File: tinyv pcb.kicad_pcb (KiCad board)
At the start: 2 copper layers, 208.8 x 80.2 mm, 102 parts, among them J1 JST SH, J2 Pico EZmate, J5 Conn_01x09_Socket, J6 Conn_01x09_Socket, Q1 2N7002, SW1 RST, U1 STM32F072C8Tx, U2 MCP1700x-330xxTT, U4 USBLC6-2SC6

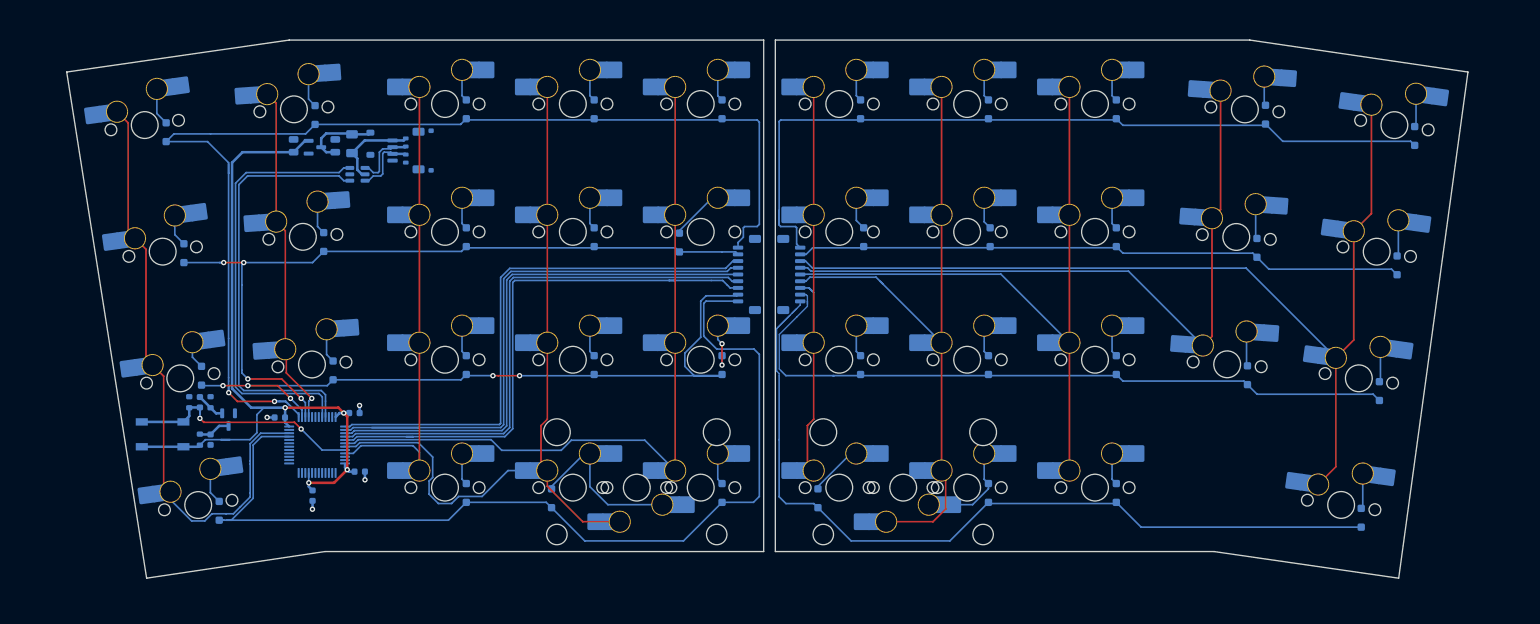
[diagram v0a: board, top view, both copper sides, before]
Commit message: routing improvements, error check, cleanup
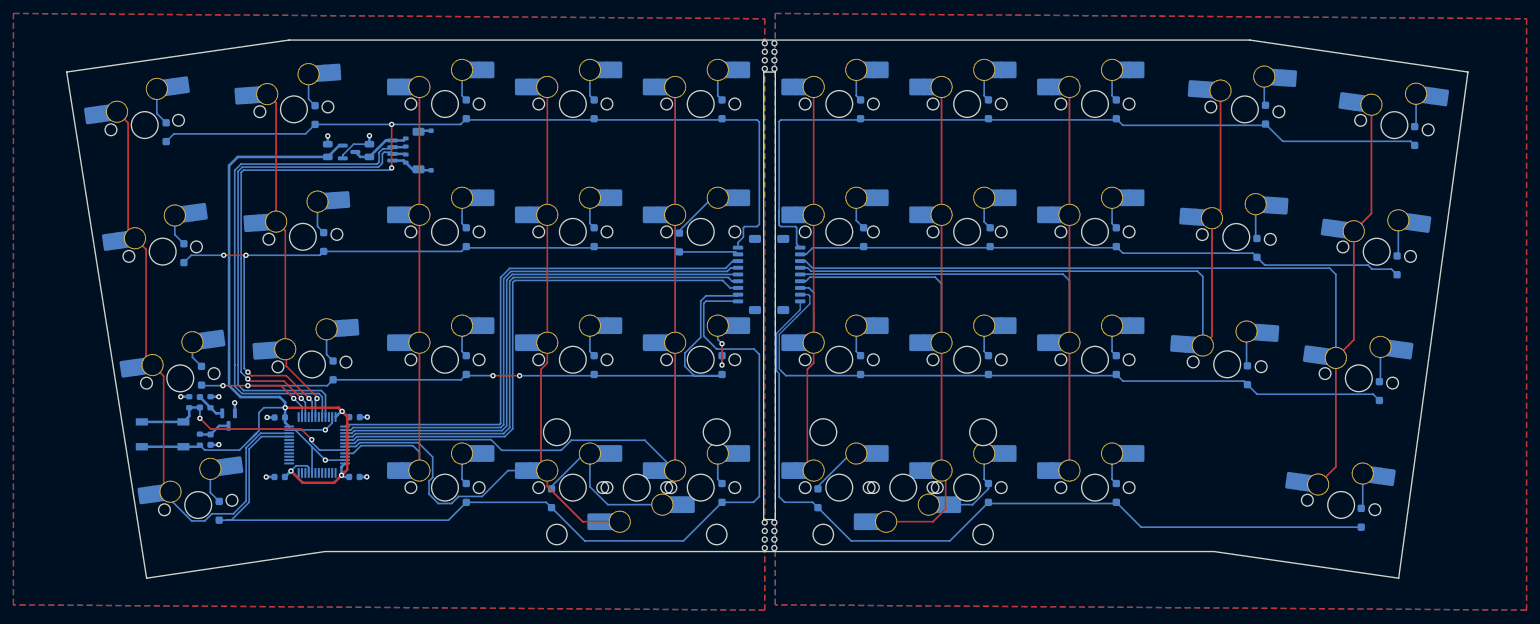
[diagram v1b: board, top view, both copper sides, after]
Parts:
- removed D_PWR1: SMF9.0CA, Diode_SMD:D_SOD-123
- removed F1: 500mA, Fuse:Fuse_1206_3216Metric
- removed U4: USBLC6-2SC6, Package_TO_SOT_SMD:SOT-23-6
- added REF**: mousebites 1mm, PCM_marbastlib-various:mousebites_1mm, F.Cu at (154.1, 23.8)
- added REF**: mousebites 1mm, PCM_marbastlib-various:mousebites_1mm, F.Cu at (152.2, 95.2)
- added REF**: mousebites 1mm, PCM_marbastlib-various:mousebites_1mm, F.Cu at (152.2, 23.8)
- added REF**: mousebites 1mm, PCM_marbastlib-various:mousebites_1mm, F.Cu at (154.1, 95.2)
- moved C5 5.63 mm to (80.2, 86.5), turned to 180 degrees
- moved U2 5.14 mm to (90.5, 38.1)
- moved C1 5.14 mm to (93.5, 37.9)
- moved C2 5.14 mm to (87.3, 37.9)
- moved C4 1.12 mm to (91.3, 86.5)
- moved C6 0.62 mm to (91.3, 77.6)
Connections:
- J1 pad 1: VBUS -> +5V
- J1 pad 2: D_USB_N -> D_N
- J1 pad 3: D_USB_P -> D_P
- J2 pad 1: VBUS -> +5V
- J2 pad 2: D_USB_N -> D_N
- J2 pad 3: D_USB_P -> D_P
- U1 pad 25: ROW0 -> unconnected-(U1-PB12-Pad25)
- U1 pad 27: ROW1 -> ROW0
- U1 pad 28: COL1 -> unconnected-(U1-PB15-Pad28)
- U1 pad 29: unconnected-(U1-PA8-Pad29) -> ROW1
- U1 pad 30: unconnected-(U1-PA9-Pad30) -> COL1
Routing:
- net GND: track 4.71 -> 46.7 mm, vias 4 -> 12
- net +3V3: track 118.4 -> 133.6 mm
- net VBUS: track 13.2 -> 0.00 mm
- net D_P: track 64.1 -> 75.9 mm
- net D_N: track 65.1 -> 76.9 mm
- net ROW0: track 293.5 -> 303.9 mm, vias 2 -> 4
- net D_USB_P: track 9.75 -> 0.00 mm
- net D_USB_N: track 9.64 -> 0.00 mm
- net COL9: track 227.2 -> 234.4 mm
- net COL7: track 182.6 -> 188.0 mm
- net COL6: track 180.1 -> 184.7 mm
- net ROW3: track 274.9 -> 270.8 mm
- net COL5: track 151.7 -> 149.3 mm
- net +5V: track 11.3 -> 8.96 mm
- net ROW1: track 205.3 -> 206.7 mm
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- added copper zone on B.Cu, net GND
- added copper zone on F.Cu, net GND
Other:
- outline, holes or cut-outs redrawn
